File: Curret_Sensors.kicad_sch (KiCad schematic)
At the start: 15 parts, among them U1 INA282, U2 INA282, U3 INA282

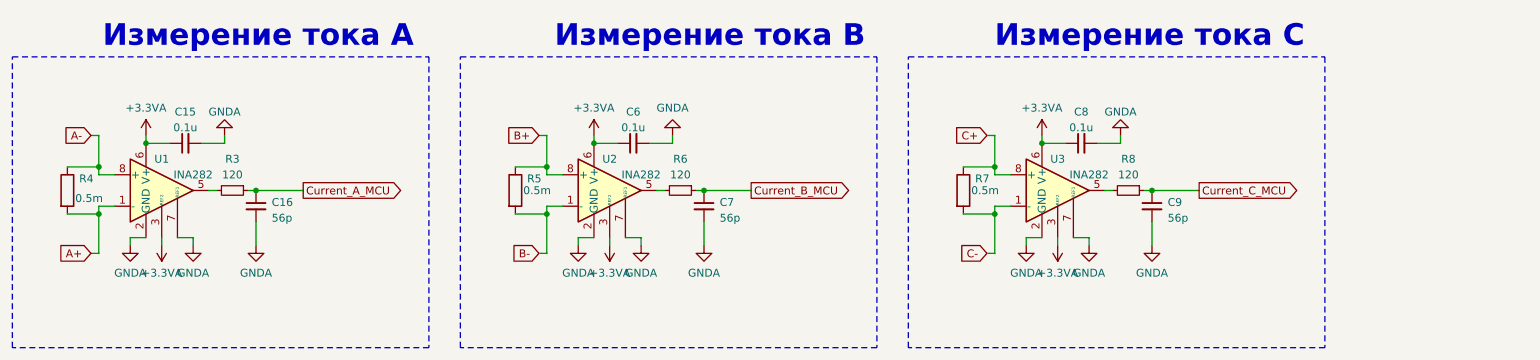
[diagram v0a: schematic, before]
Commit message: Датчики тока NSM2015
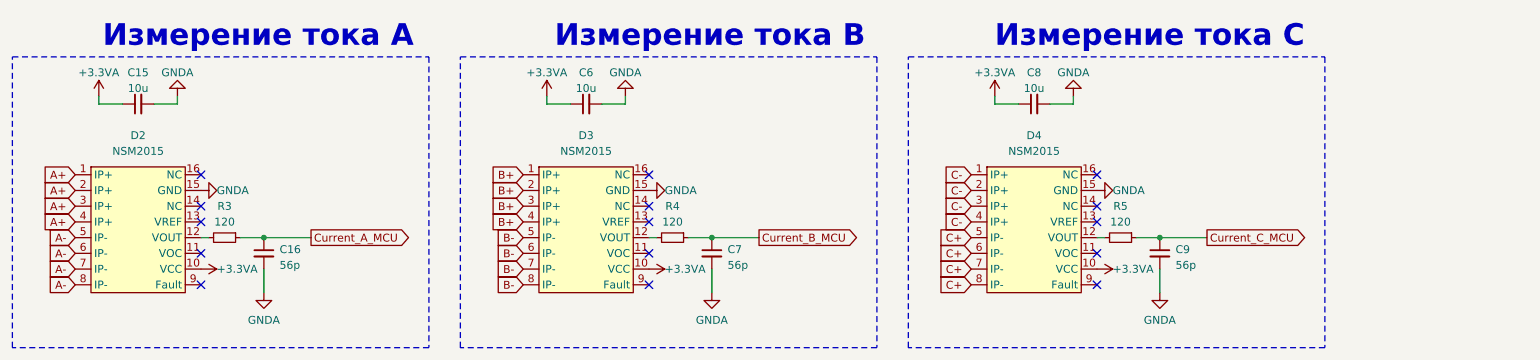
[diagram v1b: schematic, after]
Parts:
- removed R4, R5, R7: 0.5m, Resistor_SMD:R_2512_6332Metric_Pad1.40x3.35mm_HandSolder, symbol Device:R
- removed R6, R8: 120, Resistor_SMD:R_0603_1608Metric_Pad0.98x0.95mm_HandSolder, symbol Device:R_Small
- removed U1, U2, U3: INA282, Package_SO:SOIC-8_3.9x4.9mm_P1.27mm, symbol Amplifier_Current:INA283
- added D2, D3, D4: NSM2015, Package_SO:SOIC-16W_7.5x10.3mm_P1.27mm, symbol Sensors_My:NSM2015
- added R4, R5: 120, Resistor_SMD:R_0603_1608Metric_Pad0.98x0.95mm_HandSolder, symbol Device:R_Small
- C15, C6, C8: value 0.1u -> 10u
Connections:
- net +3.3VA: now also D2.10 (VCC), D3.10 (VCC), D4.10 (VCC)
- net A+: now also D2.1 (IP+), D2.2 (IP+), D2.3 (IP+), D2.4 (IP+)
- net A-: now also D2.5 (IP-), D2.6 (IP-), D2.7 (IP-), D2.8 (IP-)
- net B+: now also D3.1 (IP+), D3.2 (IP+), D3.3 (IP+), D3.4 (IP+)
- net B-: now also D3.5 (IP-), D3.6 (IP-), D3.7 (IP-), D3.8 (IP-)
- net C+: now also D4.5 (IP-), D4.6 (IP-), D4.7 (IP-), D4.8 (IP-)
- net C-: now also D4.1 (IP+), D4.2 (IP+), D4.3 (IP+), D4.4 (IP+)
- net Current_B_MCU: now also R4.1
- net Current_C_MCU: now also R5.1
- net GNDA: now also D2.15 (GND), D3.15 (GND), D4.15 (GND)
- net at R3.2: now also D2.12 (VOUT)
- new net: D3.12 (VOUT), R4.2
- new net: D4.12 (VOUT), R5.2
- no-connect marks 0 -> 15
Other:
- moved on the sheet: C15, C16, R3
